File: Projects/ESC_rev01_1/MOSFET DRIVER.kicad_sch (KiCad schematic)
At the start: 0 parts

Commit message: Update 06
MOSFET DRIVER schematic created
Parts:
- added C18: 120p, symbol Device:C
- added C19: 6n8, symbol Device:C
- added C20, C21, C22, C23, C24, C25: 2u2, symbol Device:C
- added C26, C27, C28, C29, C30, C31, C32, C33, C34, C35, C36, C37: 10u, symbol Device:C
- added C38, C39, C40, C41: 100n, symbol Device:C
- added D4: PMEG6020ER, Diode_SMD:Nexperia_CFP3_SOD-123W, symbol Diode:PMEG6020ER
- added D5: BAT60A, Diode_SMD:D_SOD-323, symbol Diode:BAT60A
- added L1: 22u, symbol Device:L
- added R11: 205k, symbol Device:R
- added R12: 16k2, symbol Device:R
- added R13, R16, R18, R20: 18k, symbol Device:R
- added R14, R17, R19, R21: 3k3, symbol Device:R
- added R15: 10k, symbol Device:R
- added R22: 1M, symbol Device:R
- added U2: DRV8302DCA, DCA56_6P35X3P61, symbol DRV8302:DRV8302DCA
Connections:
- new net: C19.2, R12.1
- new net: C25.1, U2.27 (AVDD)
- new net: C24.1, U2.14 (CP1)
- new net: C24.2, U2.15 (CP2)
- new net: C22.1, C23.1, U2.13 (GVDD)
- new net: R15.2, U2.7 (DTC)
- new net +3V3: U2.24 (REF), U2.9 (M_OC)
- new net +5V: D5.1 (K)
- new net +5V_DRV: C35.1, C36.1, C37.1, D5.2 (A), L1.2, R13.1
- new net +VDC: C26.1, C27.1, C28.1, C29.1, C30.1, C31.1, C32.1, C33.1, C34.1, U2.29 (PVDD1), U2.53 (PVDD2), U2.54 (PVDD2)
- new net BIAS: R22.1, U2.49 (BIAS)
- new net BR_SO1: U2.25 (SO1)
- new net BR_SO2: U2.26 (SO2)
- new net BST_A: C39.1, U2.48 (BST_A)
- new net BST_B: C40.1, U2.43 (BST_B)
- new net BST_BK: C38.1, U2.52 (BST_BK)
- new net BST_C: C41.1, U2.38 (BST_C)
- new net COMP: C18.2, R12.2, U2.2 (COMP)
- new net DC_CAL: U2.12 (DC_CAL)
- new net DVDD: C20.1, C21.1, U2.11 (OC_ADJ), U2.23 (DVDD)
- new net EN_GATE: U2.16 (EN_GATE)
- new net FAULT: U2.6 (*FAULT)
- new net GND: C18.1, C19.1, C20.2, C21.2, C22.2, C23.2, C25.2, C26.2, C27.2, C28.2, C29.2, C30.2, C31.2, C32.2, C33.2, C34.2, C35.2, C36.2, C37.2, D4.2 (A), R11.1, R14.2, R15.1, R17.2, R19.2, R21.2, R22.2, U2.10 (GAIN), U2.28 (AGND), U2.57 (EPAD), U2.8 (M_PWM)
- new net H1: U2.17 (INH_A)
- new net H1_LOW: U2.44 (SL_A)
- new net H1_VS: C39.2, R20.1, U2.46 (SH_A)
- new net H2: U2.19 (INH_B)
- new net H2_LOW: U2.39 (SL_B)
- new net H2_VS: C40.2, R18.1, U2.41 (SH_B)
- new net H3: U2.21 (INH_C)
- new net H3_LOW: U2.34 (SL_C)
- new net H3_VS: C41.2, R16.1, U2.36 (SH_C)
- new net L1: U2.18 (INL_A)
- new net L2: U2.20 (INL_B)
- new net L3: U2.22 (INL_C)
- new net M_H1: U2.47 (GH_A)
- new net M_H2: U2.42 (GH_B)
- new net M_H3: U2.37 (GH_C)
- new net M_L1: U2.45 (GL_A)
- new net M_L2: U2.40 (GL_B)
- new net M_L3: U2.35 (GL_C)
- new net PH: C38.2, D4.1 (K), L1.1, U2.50 (PH), U2.51 (PH)
- new net RT_CLK: R11.2, U2.1 (RT_CLK)
- new net S1_N: U2.33 (SN1)
- new net S1_P: U2.32 (SP1)
- new net S2_N: U2.31 (SN2)
- new net S2_P: U2.30 (SP2)
- new net SENS1: R16.2, R17.1
- new net SENS2: R18.2, R19.1
- new net SENS3: R20.2, R21.1
- new net VSENSE: R13.2, R14.1, U2.3 (VSENSE)
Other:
- note added: "10uF Decoupling capacitors. Place one as close as possible to each pin."
- note added: "BOOTSTRAP CAPs"
- note added: "BULK CAPACITANCE KEEP AS CLOSE AS POSSIBLE TO THE IC AND TO THE DRIVER INPUT LOOP"
- note added: "Hx_VS MCU SENSING FEEDBACK FOR EACH PHASE"
- note added: "INPUT PORTS"
- note added: "KEEP AVAY FROM NOISY TRACKS AND COMPONENTS"
- note added: "MOSFET DRIVER"
- note added: "OUTPUT PORTS"
- note added: "PHASE 1"
- note added: "PHASE 2"
- note added: "PHASE 3"
- note added: "SENSE 1 - PHASE 1"
- note added: "SENSE 2 - PHASE 2"

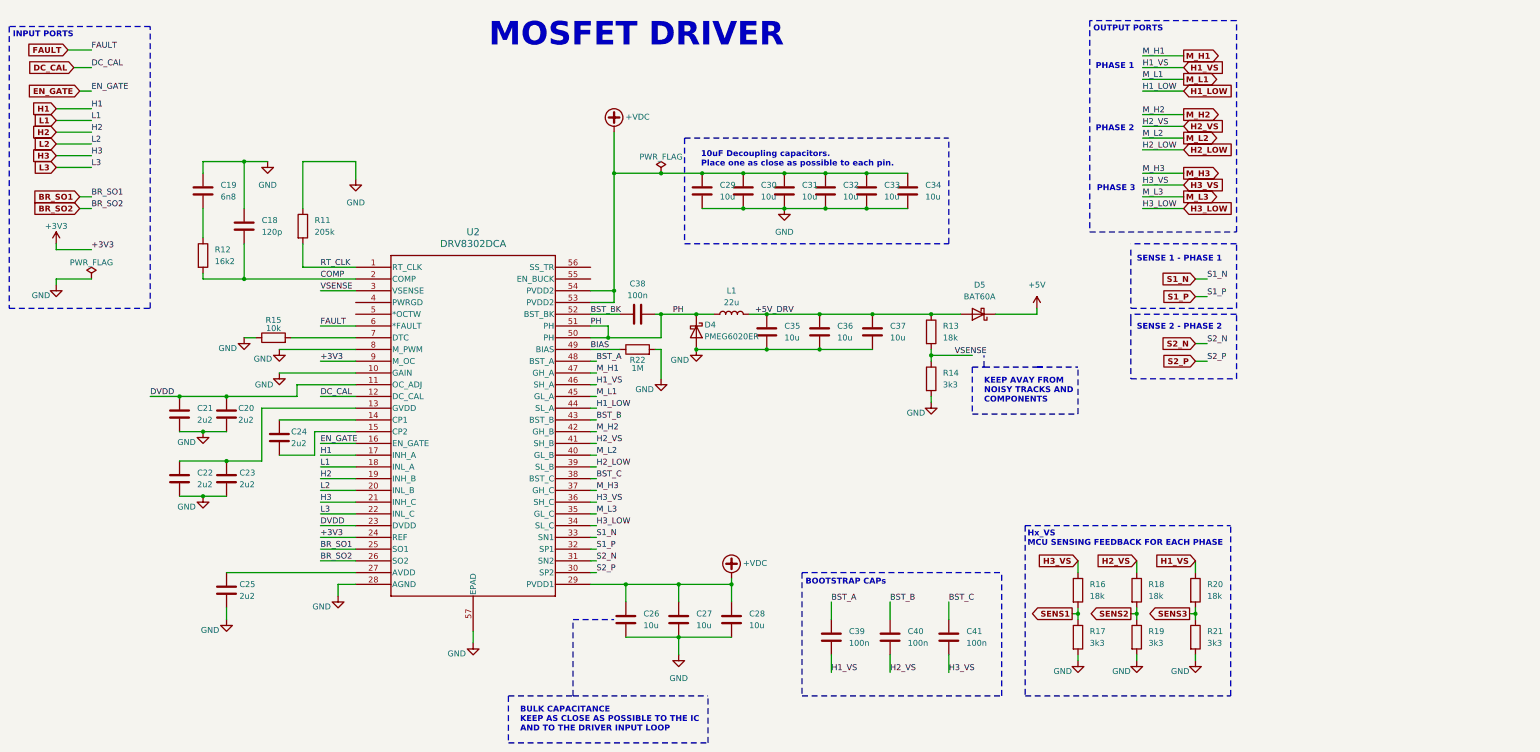
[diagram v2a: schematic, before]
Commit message: Update 07
Schematic is ready
INPUT PROTECTION schematic created
MOSFETs schematic created
CAN schematic created
FILTERs schematic created
MECHANICAL schematic created
STEP-DOWN schematic created
Footprints, 3D models are added and corrected (major issues)
Component placement started
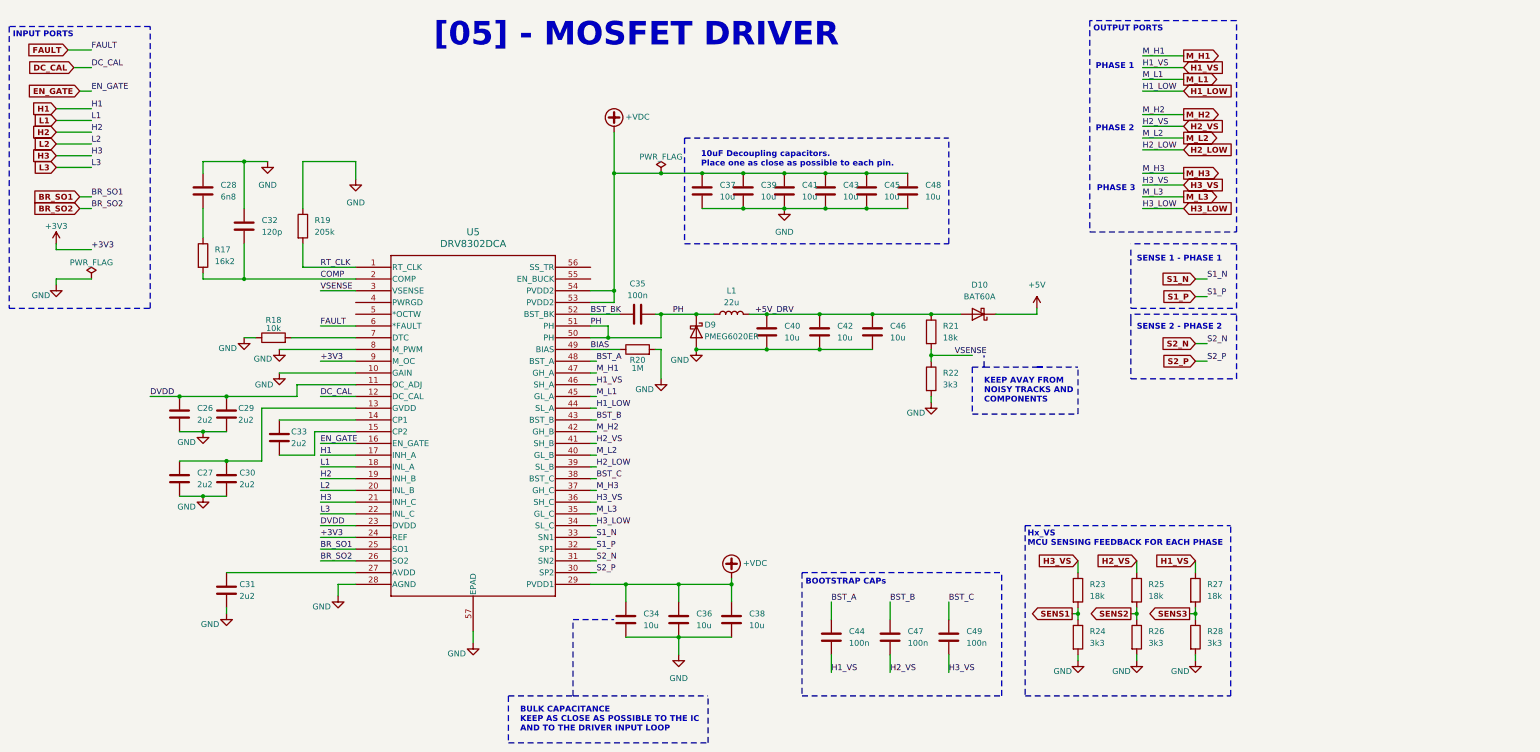
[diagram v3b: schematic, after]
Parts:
- C26: renamed from C21; footprint (none) -> Capacitor_SMD:C_0603_1608Metric
- C27: renamed from C22; footprint (none) -> Capacitor_SMD:C_0603_1608Metric
- C28: renamed from C19; footprint (none) -> Capacitor_SMD:C_0603_1608Metric
- C29: renamed from C20; footprint (none) -> Capacitor_SMD:C_0603_1608Metric
- C30: renamed from C23; footprint (none) -> Capacitor_SMD:C_0603_1608Metric
- C31: renamed from C25; footprint (none) -> Capacitor_SMD:C_0603_1608Metric
- C32: renamed from C18; footprint (none) -> Capacitor_SMD:C_0603_1608Metric
- C33: renamed from C24; footprint (none) -> Capacitor_SMD:C_0603_1608Metric
- C34: renamed from C26; footprint (none) -> Capacitor_SMD:C_0603_1608Metric
- C35: renamed from C38; footprint (none) -> Capacitor_SMD:C_0603_1608Metric
- C36: renamed from C27; footprint (none) -> Capacitor_SMD:C_0603_1608Metric
- C37: renamed from C29; footprint (none) -> Capacitor_SMD:C_0603_1608Metric
- C38: renamed from C28; footprint (none) -> Capacitor_SMD:C_0603_1608Metric
- C39: renamed from C30; footprint (none) -> Capacitor_SMD:C_0603_1608Metric
- C40: renamed from C35; footprint (none) -> Capacitor_SMD:C_0603_1608Metric
- C41: renamed from C31; footprint (none) -> Capacitor_SMD:C_0603_1608Metric
- C42: renamed from C36; footprint (none) -> Capacitor_SMD:C_0603_1608Metric
- C43: renamed from C32; footprint (none) -> Capacitor_SMD:C_0603_1608Metric
- C44: renamed from C39; footprint (none) -> Capacitor_SMD:C_0603_1608Metric
- C45: renamed from C33; footprint (none) -> Capacitor_SMD:C_0603_1608Metric
- C46: renamed from C37; footprint (none) -> Capacitor_SMD:C_0603_1608Metric
- C47: renamed from C40; footprint (none) -> Capacitor_SMD:C_0603_1608Metric
- C48: renamed from C34; footprint (none) -> Capacitor_SMD:C_0603_1608Metric
- C49: renamed from C41; footprint (none) -> Capacitor_SMD:C_0603_1608Metric
- L1: footprint (none) -> DF_ESC_rev01_1:IND-SMD_L7.8-W7.8_SDR0805
- R17: renamed from R12; footprint (none) -> Resistor_SMD:R_0603_1608Metric
- R18: renamed from R15; footprint (none) -> Resistor_SMD:R_0603_1608Metric
- R19: renamed from R11; footprint (none) -> Resistor_SMD:R_0603_1608Metric
- R20: renamed from R22; footprint (none) -> Resistor_SMD:R_0603_1608Metric
- R21: renamed from R13; footprint (none) -> Resistor_SMD:R_0603_1608Metric
- R22: renamed from R14; footprint (none) -> Resistor_SMD:R_0603_1608Metric
- R23: renamed from R16; footprint (none) -> Resistor_SMD:R_0603_1608Metric
- R24: renamed from R17; footprint (none) -> Resistor_SMD:R_0603_1608Metric
- R25: renamed from R18; footprint (none) -> Resistor_SMD:R_0603_1608Metric
- R26: renamed from R19; footprint (none) -> Resistor_SMD:R_0603_1608Metric
- R27: renamed from R20; footprint (none) -> Resistor_SMD:R_0603_1608Metric
- R28: renamed from R21; footprint (none) -> Resistor_SMD:R_0603_1608Metric
- U5: renamed from U2; footprint DCA56_6P35X3P61 -> DF_ESC_rev01_1:DCA56_6P35X3P61
- renumbered D5 to D10, D4 to D9
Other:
- note added: "[05] - MOSFET DRIVER"
- note removed: "MOSFET DRIVER"

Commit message: Update 09
Components placement finished
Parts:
- renumbered C26 to C24, C27 to C25, C28 to C26, C29 to C27, C30 to C28, C31 to C29, C32 to C30, C33 to C31, C34 to C32, C35 to C33, C36 to C34, C37 to C35, C38 to C36, C39 to C37, C40 to C38, C41 to C39, C42 to C40, C43 to C41, C44 to C42, C45 to C43, C46 to C44, C47 to C45, C48 to C46, C49 to C47, D9 to D13, D10 to D14, R17 to R14, R18 to R15, R19 to R16, R20 to R17, R21 to R18, R22 to R19, R23 to R20, R24 to R21, R25 to R22, R26 to R23, R27 to R24, R28 to R25, U5 to U3

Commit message: Update 12
Continue routing
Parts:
- added NT9: NetTie_2, NetTie:NetTie-2_SMD_Pad0.5mm, symbol Device:NetTie_2
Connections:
- net DVDD: now also NT9.1; no longer C24.1, C27.1, U3.11 (OC_ADJ)
- net CP1: now reaches C31.1, U3.14 (CP1)
- net CP2: now reaches C31.2, U3.15 (CP2)
- net DTC: now reaches R15.2, U3.7 (DTC)
- new net OC_ADJ: C24.1, C27.1, NT9.2, U3.11 (OC_ADJ)
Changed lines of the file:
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@@
 	(wire
 		(pts
+			(xy 49.53 97.79) (xy 53.34 97.79)
+		)
+		(stroke
+			(width 0)
+			(type default)
+		)
+	)
+	(wire
+		(pts
 			(xy 161.29 142.24) (xy 161.29 138.43)
 		)
@@
 	(wire
 		(pts
-			(xy 46.99 97.79) (xy 53.34 97.79)
+			(xy 38.1 97.79) (xy 44.45 97.79)
 		)
 		(stroke
@@
 		)
 	)
+	(label "OC_ADJ"
+		(at 83.82 95.25 0)
+		(effects
+			(font
+				(size 1.27 1.27)
+				(thickness 0.1588)
+			)
+			(justify left bottom)
+		)
+	)
 	(label "PH"
 		(at 142.24 82.55 0)
@@
 		)
 	)
+	(label "DTC"
+		(at 83.82 85.09 0)
+		(effects
+			(font
+				(size 1.27 1.27)
+				(thickness 0.1588)
+			)
+			(justify left bottom)
+		)
+	)
 	(label "M_L3"
 		(at 261.62 54.61 0)
@@
 		)
 	)
+	(label "CP1"
+		(at 83.82 102.87 0)
+		(effects
+			(font
+				(size 1.27 1.27)
+				(thickness 0.1588)
+			)
+			(justify left bottom)
+		)
+	)
 	(label "DC_CAL"
 		(at 83.82 97.79 0)
@@
 		)
 	)
+	(label "CP2"
+		(at 83.82 105.41 0)
+		(effects
+			(font
+				(size 1.27 1.27)
+				(thickness 0.1588)
+			)
+			(justify left bottom)
+		)
+	)
 	(label "BST_A"
 		(at 194.31 142.24 0)
@@
 	)
 	(label "DVDD"
-		(at 46.99 97.79 0)
+		(at 38.1 97.79 0)
 		(effects
 			(font
@@
 					(unit 1)
 				)
+			)
+		)
+	)
+	(symbol
+		(lib_id "Device:NetTie_2")
+		(at 46.99 97.79 0)
+		(unit 1)
+		(exclude_from_sim no)
+		(in_bom no)
+		(on_board yes)
+		(dnp no)
+		(fields_autoplaced yes)
+		(property "Reference" "NT9"
+			(at 46.99 92.71 0)
+			(effects
+				(font
+					(size 1.27 1.27)
+				)
+			)
+		)
+		(property "Value" "NetTie_2"
+			(at 46.99 95.25 0)
+			(effects
+				(font
+					(size 1.27 1.27)
+				)
+			)
+		)
+		(property "Footprint" "NetTie:NetTie-2_SMD_Pad0.5mm"
+			(at 46.99 97.79 0)
+			(effects
+				(font
+					(size 1.27 1.27)
+				)
+				(hide yes)
+			)
+		)
+		(property "Datasheet" "~"
+			(at 46.99 97.79 0)
+			(effects
+				(font
+					(size 1.27 1.27)
+				)
+				(hide yes)
+			)
+		)
+		(property "Description" "Net tie, 2 pins"
+			(at 46.99 97.79 0)
+			(effects
+				(font
+					(size 1.27 1.27)
+				)
+				(hide yes)
+			)
+		)
+		(pin "1"
+		)
+		(pin "2"
+		)
+		(instances
+			(project ""
+				(path "/e63e39d7-6ac0-4ffd-8aa3-1841a4541b55/6dc0778c-071b-4174-a187-40a7d7e16416"
+					(reference "NT9")
+					(unit 1)
+				)

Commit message: Update 01
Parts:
- C24, C25, C27, C28, C29, C31: value 2u2 -> C
- C26: value 6n8 -> C
- C30: value 120p -> C
- C32, C34, C35, C36, C37, C38, C39, C40, C41, C43, C44, C46: value 10u -> C
- C33, C42, C45, C47: value 100n -> C
- L1: value 22u -> L; footprint DF_ESC_rev01_1:IND-SMD_L7.8-W7.8_SDR0805 -> KeIr_lib:IND-SMD_L7.8-W7.8_SDR0805
- R14: value 16k2 -> R
- R15: value 10k -> R
- R16: value 205k -> R
- R17: value 1M -> R
- R18, R20, R22, R24: value 18k -> R
- R19, R21, R23, R25: value 3k3 -> R
- U3: footprint DF_ESC_rev01_1:DCA56_6P35X3P61 -> KeIr_lib:HTSSOP-56_L14.0-W6.0-P0.50-LS8.0-BL
- renumbered NT9 to NT1
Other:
- note added: "1uF or 10uF Decoupling capacitors?"
- note added: "BOOTSTRAP CAPs for current sensing of each phase"
- note added: "FEEDBACK SIGNAL"
- note added: "FILTER reducing ripple and noize"
- note added: "KEEP AVAY FROM NOISY TRACKS AND COMPONENTS its affect the operation of buck converter"
- note removed: "BOOTSTRAP CAPs"
- note removed: "KEEP AVAY FROM NOISY TRACKS AND COMPONENTS"
- title: (none) -> DF_ESC_rev01_1
- moved on the sheet: C42, C45, C47
